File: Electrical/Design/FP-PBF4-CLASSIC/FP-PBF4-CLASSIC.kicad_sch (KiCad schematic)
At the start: 26 parts

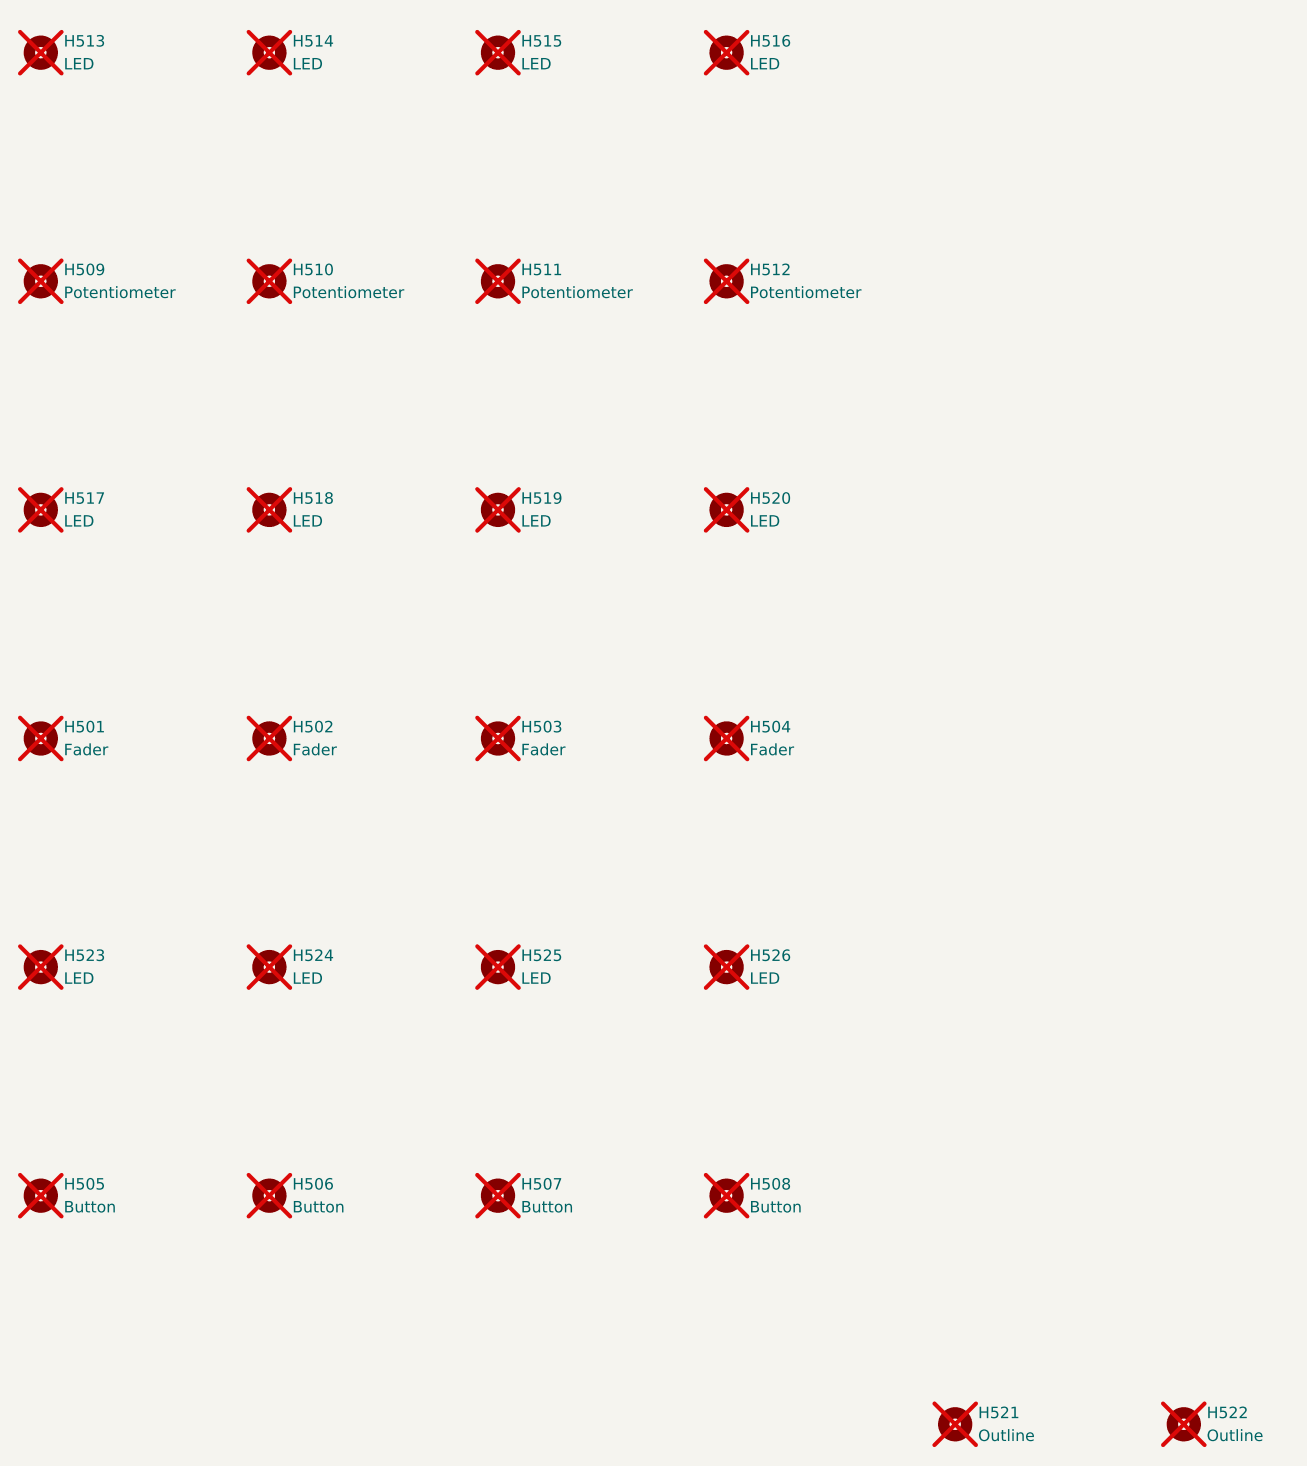
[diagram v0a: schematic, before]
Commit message: SUKU rest of the frontpanels updated to use the plated through-hole for lightpipe
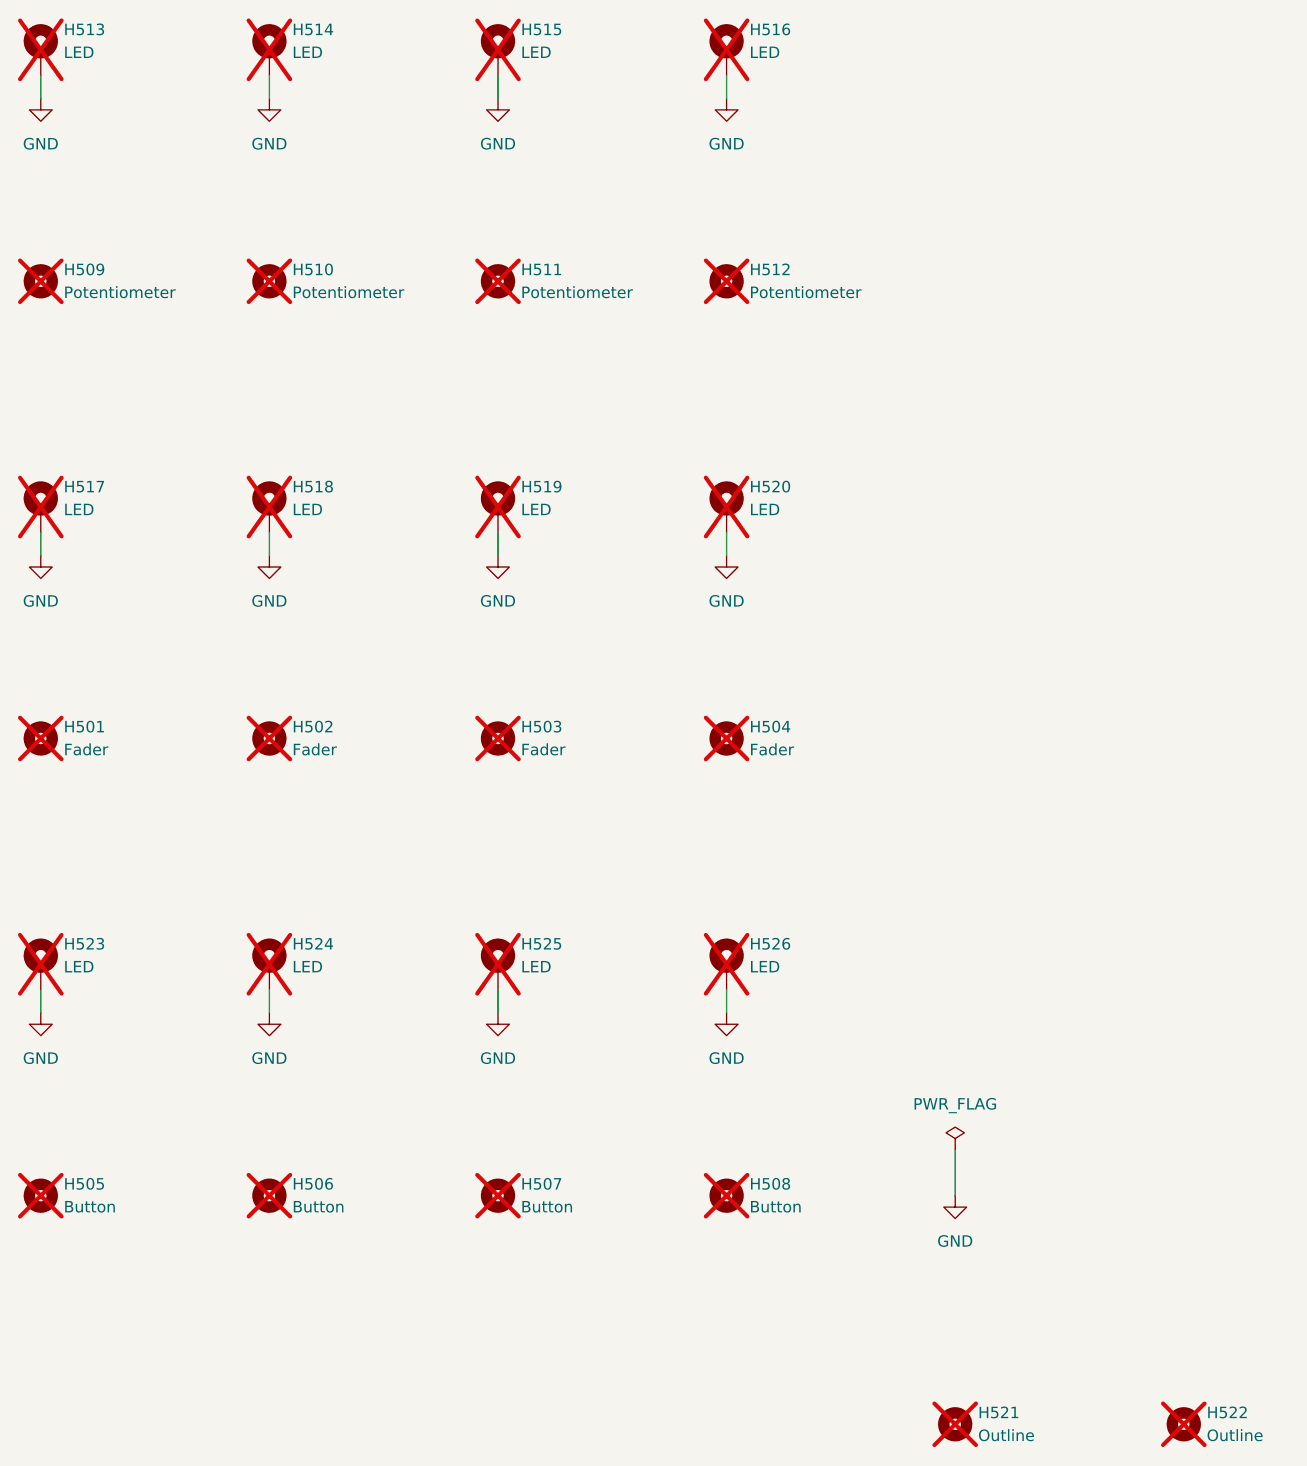
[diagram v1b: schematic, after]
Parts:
- H513, H514, H515, H516, H517, H518, H519, H520, H523, H524, H525, H526: footprint suku_basics:FP_LED -> suku_basics:FP_LED_TIGHT; symbol Mechanical:MountingHole -> Mechanical:MountingHole_Pad
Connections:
- new net GND: H513.1, H514.1, H515.1, H516.1, H517.1, H518.1, H519.1, H520.1, H523.1, H524.1, H525.1, H526.1
